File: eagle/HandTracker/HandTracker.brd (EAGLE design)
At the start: 82.5 x 100 mm, 29 parts, among them IC1 FT232RL, J1 ZX62-AB-5PA(31), U1 LSM9DS1TR, U2 MAX11629EEE+21-0055_E16+5_MXM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

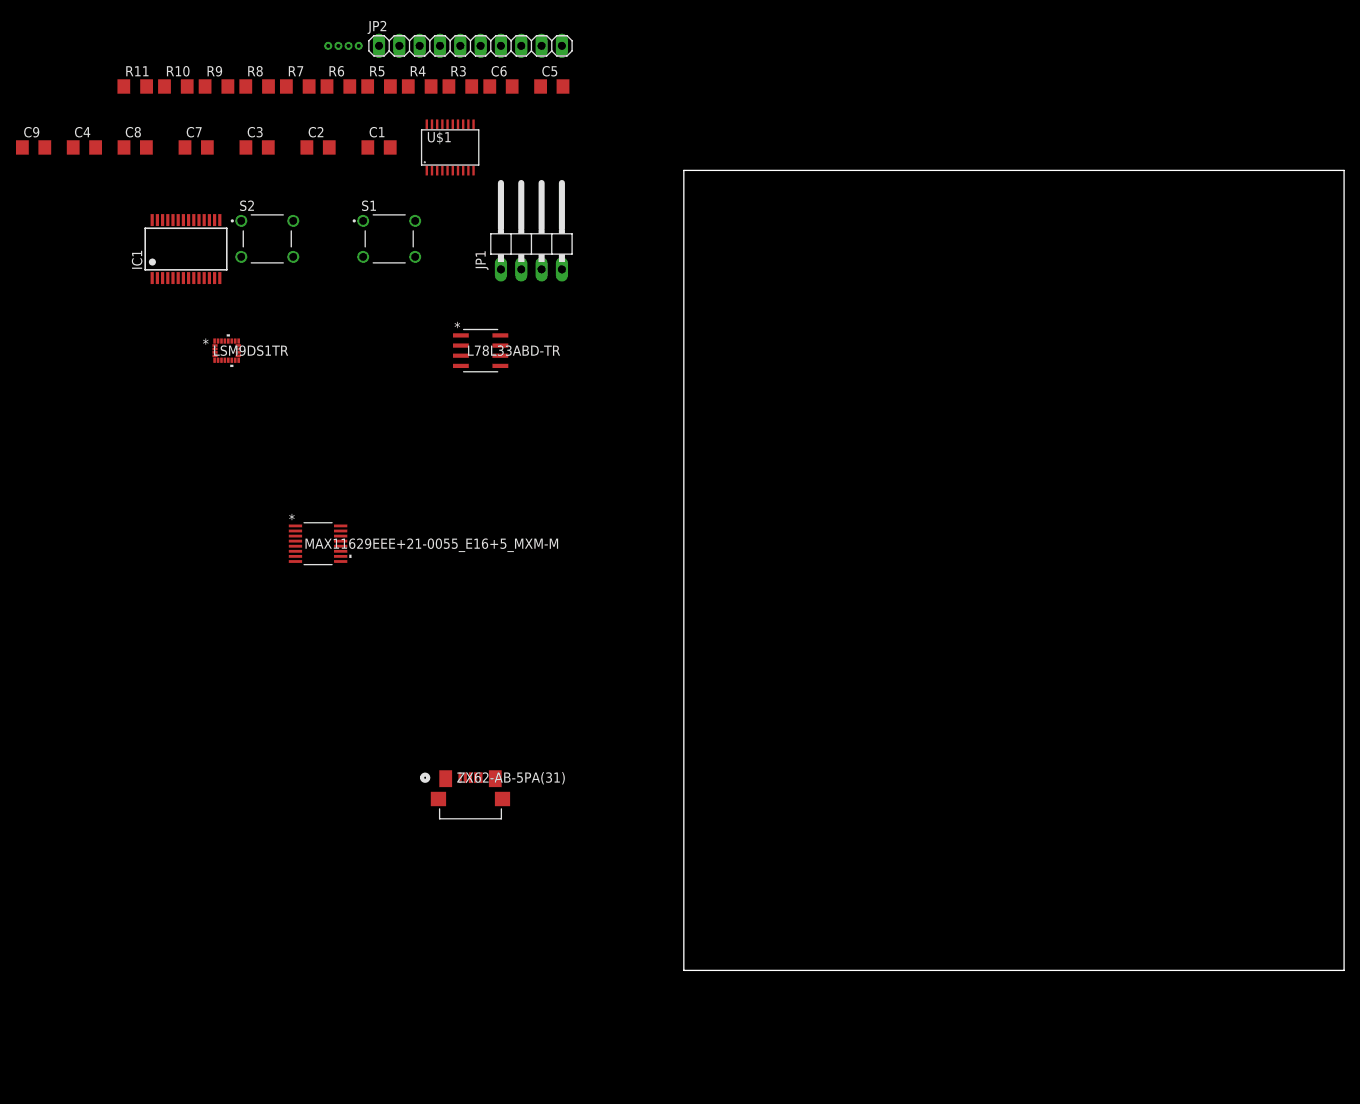
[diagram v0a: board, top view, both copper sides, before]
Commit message: Board routing minus VDD and GND planes.
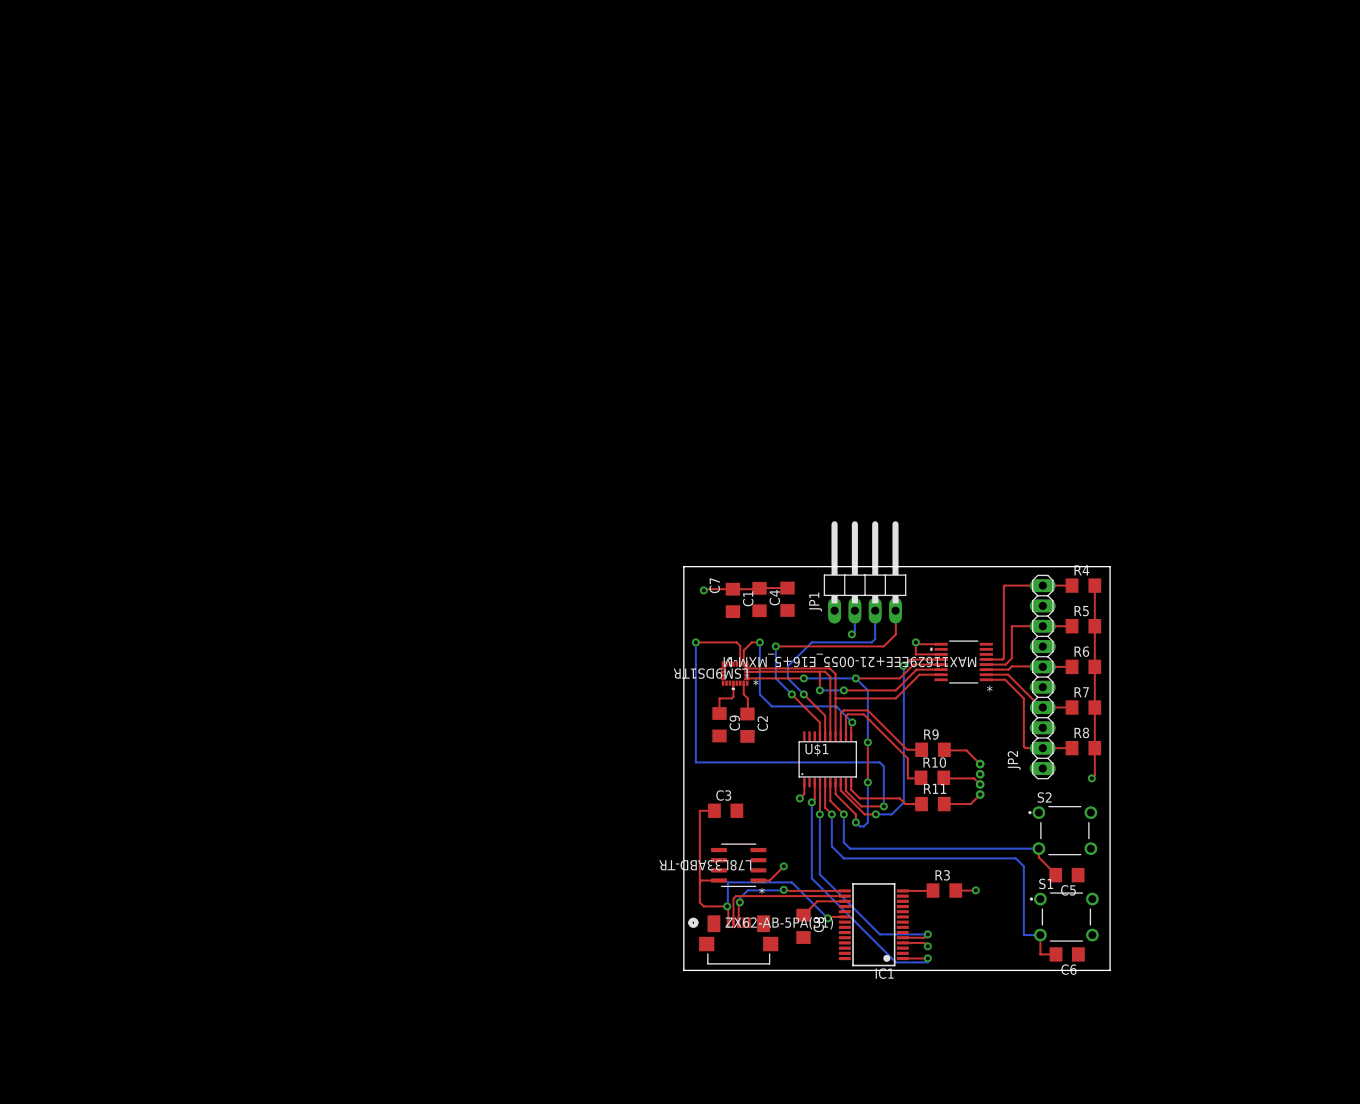
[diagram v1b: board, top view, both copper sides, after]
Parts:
- moved R11 134.1 mm to (31.1, 20.8)
- moved R8 132.3 mm to (50.0, 27.8)
- moved C6 129.5 mm to (47.9, 2.00), turned to 180 degrees
- moved C8 128.3 mm to (15.0, 5.51), turned to 270 degrees
- moved R10 128.1 mm to (31.1, 24.1)
- moved R7 125.2 mm to (50.0, 32.9)
- moved S2 124.1 mm to (47.6, 17.5)
- moved U$2 124.1 mm to (37.0, 22.0), turned to 90 degrees
- moved R9 122.1 mm to (31.1, 27.6)
- moved IC1 120.5 mm to (23.8, 5.71), turned to 90 degrees
- moved S1 119.8 mm to (47.8, 6.67)
- moved R6 118.1 mm to (50.0, 37.9)
- moved C5 117.7 mm to (47.9, 11.9), turned to 180 degrees
- moved R3 117.3 mm to (32.6, 9.98)
- moved C9 112.1 mm to (4.46, 30.7), turned to 270 degrees
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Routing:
- net CSM: track 0.00 -> 58.3 mm, vias 0 -> 2
- net VCC: track 0.00 -> 57.9 mm, vias 0 -> 8
- net SCLK: track 0.00 -> 51.6 mm, vias 0 -> 5
- net SW1: track 0.00 -> 48.3 mm, vias 0 -> 1
- net VBUS: track 0.00 -> 40.7 mm, vias 0 -> 2
- net SW2: track 0.00 -> 37.1 mm, vias 0 -> 1
- net MOSI: track 0.00 -> 36.7 mm, vias 0 -> 2
- net RX3V3: track 0.00 -> 34.6 mm, vias 0 -> 2
- net MISO: track 0.00 -> 34.1 mm
- net CSA: track 0.00 -> 32.9 mm, vias 0 -> 2
- net TEST: track 0.00 -> 32.1 mm, vias 0 -> 2
- net TX3V3: track 0.00 -> 31.4 mm, vias 0 -> 2
- net RST: track 0.00 -> 26.5 mm, vias 0 -> 1
- net CSAG: track 0.00 -> 25.4 mm, vias 0 -> 2
- net GLED: track 0.00 -> 21.7 mm
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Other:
- board size 82.5 x 100 mm -> 53.3 x 50.5 mm

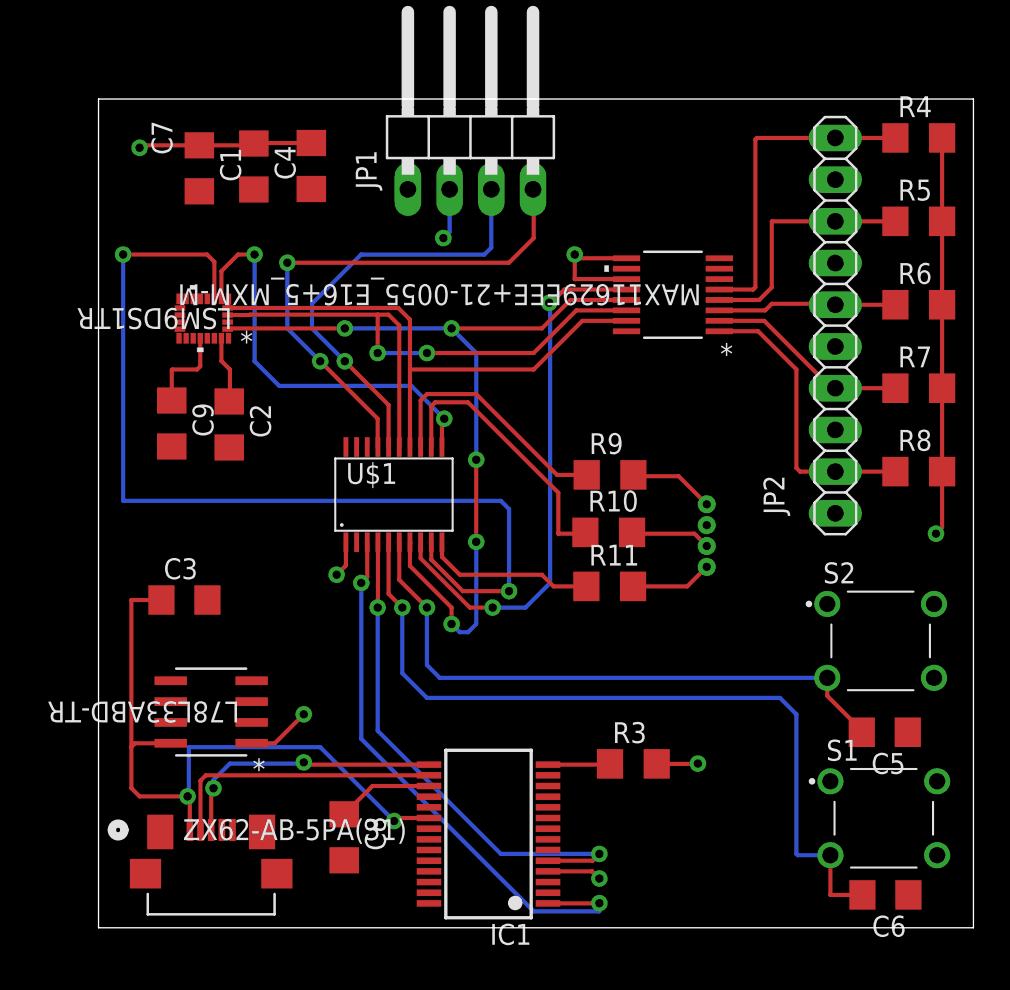
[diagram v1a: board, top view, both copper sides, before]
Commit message: Draft 1 PCB with GND and VCC planes.
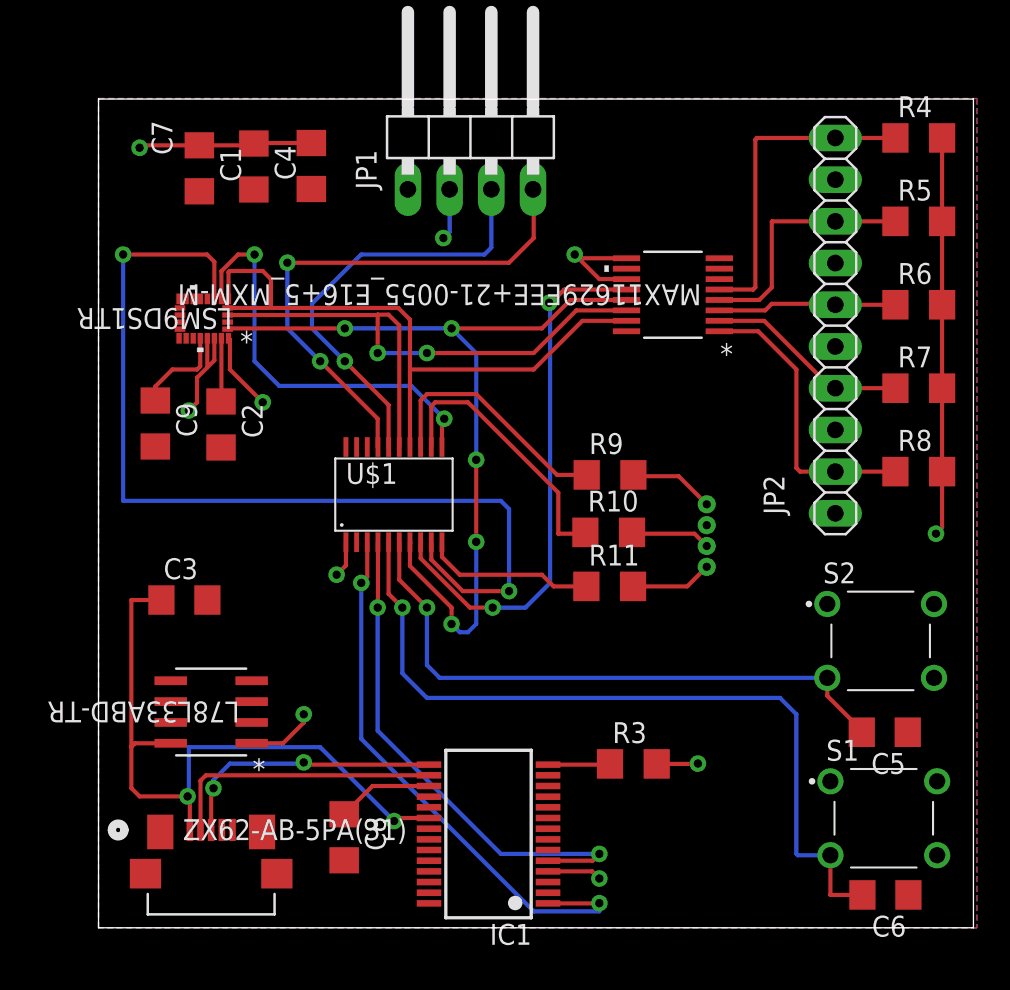
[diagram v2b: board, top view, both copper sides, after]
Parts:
- moved C9 1.00 mm to (3.46, 30.7)
- moved C2 0.50 mm to (7.46, 30.6)
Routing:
- net VCC: track 57.9 -> 68.6 mm, vias 8 -> 10
- net MISO: track 34.1 -> 39.8 mm
- added copper zone on layer 1, net GND
- added copper zone on layer 16, net VCC

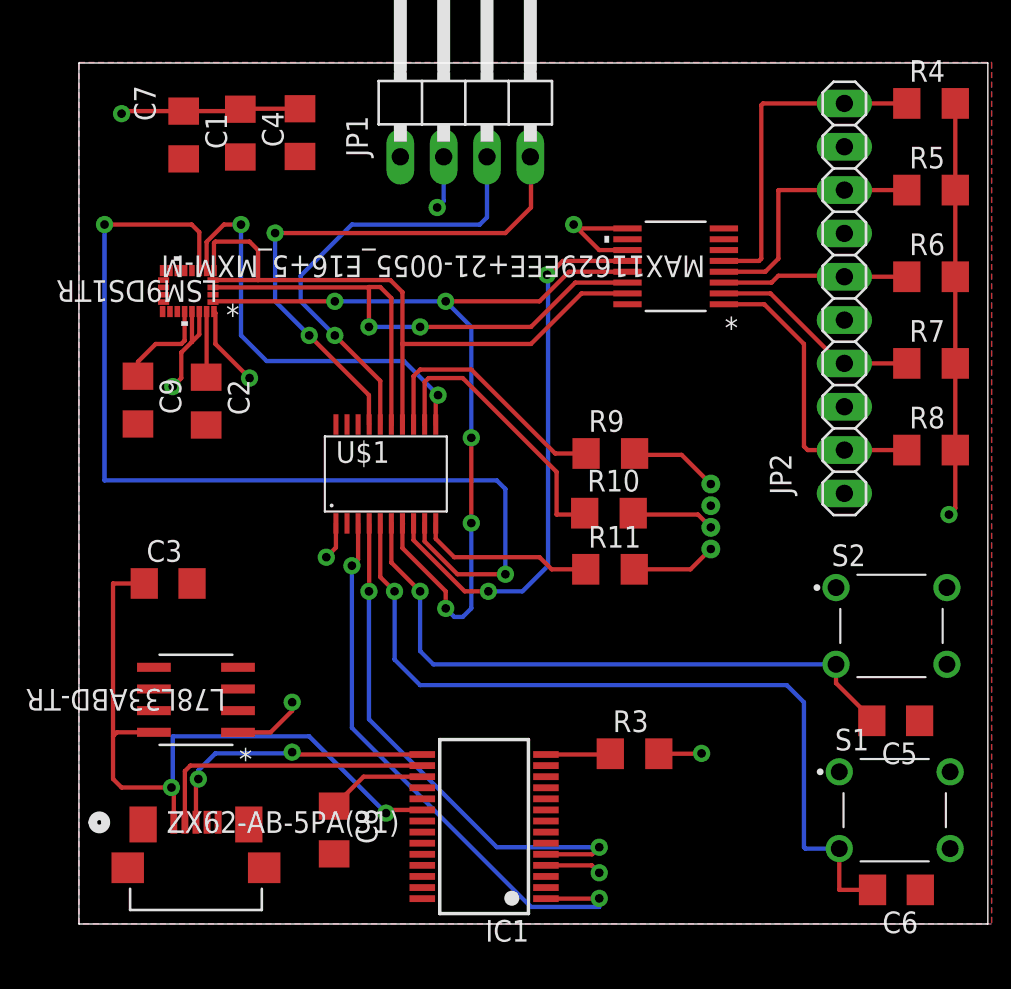
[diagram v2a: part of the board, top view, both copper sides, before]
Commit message: Fix LED and route planes.
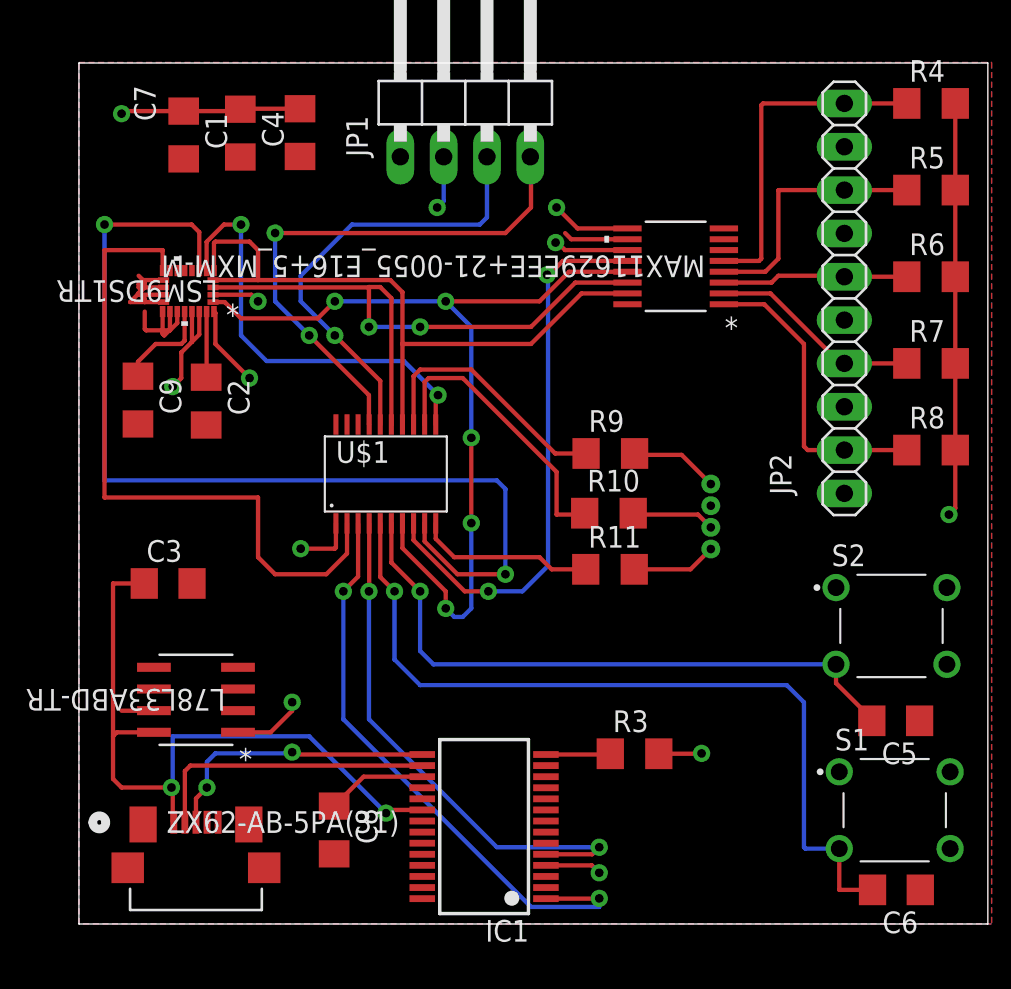
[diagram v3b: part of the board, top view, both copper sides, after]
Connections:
- new net BLED_RES: R11.2, U$2.P$1
- new net GLED_RES: R10.2, U$2.P$2
- new net RLED_RES: R9.2, U$2.P$4
- net BLED: no longer R11.2, U$2.P$1
- net DEN_AG: now also U$1.2
- net GLED: no longer R10.2, U$2.P$2
- net RLED: no longer R9.2, U$2.P$4
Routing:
- net DEN_AG: track 0.00 -> 39.5 mm
- net GND: track 0.00 -> 21.9 mm
- net VCC: track 68.6 -> 75.1 mm, vias 10 -> 12
- net RLED_RES: track 0.00 -> 5.21 mm
- net RLED: track 20.4 -> 15.1 mm
- net BLED_RES: track 0.00 -> 4.98 mm
- net BLED: track 15.4 -> 10.4 mm
- net GLED: track 21.7 -> 16.8 mm
- net GLED_RES: track 0.00 -> 4.89 mm
- net SCLK: track 51.6 -> 52.4 mm
- net VBUS: track 40.7 -> 41.2 mm
- net D-: track 16.5 -> 17.0 mm
